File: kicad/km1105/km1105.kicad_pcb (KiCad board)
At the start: 2 copper layers, 131.7 x 80 mm, 42 parts, among them J1 CONN-DEC-DOUBLE, J2 display_switches_hdr, J3 pgm_hdr, Q1 BC547, U1 ATtiny1616-S, U2 PCF8574T, U3 PCF8574T, U4 PCF8574T, U5 PCF8574T, U6 PCF8574T, U7 PCF8574T, U8 74ACT00SC, U9 LD1117S33TR_SOT223

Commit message: Update the display board
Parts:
- added C12: 100nF, Capacitor_SMD:C_0805_2012Metric, F.Cu at (221.7, 258.8)
- added J4: la_01, Connector_PinHeader_2.54mm:PinHeader_2x20_P2.54mm_Vertical, F.Cu at (325.9, 239.5)
- added J5: la_02, Connector_PinHeader_2.54mm:PinHeader_2x04_P2.54mm_Vertical, F.Cu at (325.6, 250.4)
- added U10: SN74LVC245APW, Package_SO:TSSOP-20_4.4x6.5mm_P0.65mm, F.Cu at (227.8, 258.6)
- C10, C11: footprint Capacitor_SMD:CP_Elec_8x5.4 -> Capacitor_SMD:CP_Elec_4x4.5
- G***: moved to B.Cu
- moved J3 30.5 mm to (252.5, 246.4)
- moved D1 15.8 mm to (267.9, 246.6)
- moved D2 15.8 mm to (267.9, 240.3)
- moved R10 15.8 mm to (262.2, 246.6)
- moved R11 15.8 mm to (262.2, 240.3)
- moved G*** 8.57 mm to (306.8, 261.1), turned to 180 degrees
- moved C10 3.82 mm to (240.8, 258.8)
- moved R2 3.05 mm to (267.1, 252.0)
- moved R5 3.05 mm to (267.1, 257.0)
- moved R7 3.05 mm to (267.1, 262.1)
- moved R8 3.05 mm to (267.1, 267.2)
- moved R1 3.05 mm to (262.0, 252.0)
- moved R4 3.05 mm to (262.0, 257.0)
- moved R6 3.05 mm to (262.0, 262.1)
- moved R9 3.05 mm to (262.0, 267.2)
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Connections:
- J2 pad 10: /LCD_CS -> GND
- J2 pad 11: /s4_off -> /LCD_SCK
- J2 pad 12: /LCD_DC -> GND
- J2 pad 13: /s4_on -> /LCD_MOSI
- J2 pad 14: /LCD_RST -> GND
- J2 pad 15: /+3.3V -> /LCD_RST
- J2 pad 16: /PB4 -> GND
- J2 pad 17: /+3.3V -> /LCD_DC
- J2 pad 18: /PB5 -> GND
- J2 pad 19: GND -> /LCD_CS
- J2 pad 2: +5V -> /+3.3V
- J2 pad 4: /LCD_SDA_MOSI -> /+3.3V
- J2 pad 6: /MISO -> /s4_off
- J2 pad 8: /LCD_SCK -> /s4_on
- R7 pad 2: /s4_off -> /s4_on
- R9 pad 2: /s4_on -> /s4_off
- U1 pad 17: /LCD_SDA_MOSI -> /LCDU_MOSI
- U1 pad 19: /LCD_SCK -> /LCDU_SCK
- U1 pad 2: /LCD_CS -> /LCDU_CS
- U1 pad 8: /LCD_RST -> /LCDU_RST
- U1 pad 9: /LCD_DC -> /LCDU_DC
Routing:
- net /BSR14_H_2: track 42.0 -> 173.4 mm, vias 1 -> 4
- net /BSR7_H_2: track 31.3 -> 154.8 mm, vias 1 -> 2
- net /C_H_2: track 13.8 -> 134.0 mm
- net /BSR12_H_2: track 33.2 -> 153.2 mm, vias 1 -> 5
- net /BSR8_H_2: track 31.8 -> 148.8 mm, vias 1 -> 4
- net /BSR15_H_2: track 19.0 -> 132.1 mm, vias 1 -> 2
- net /ISR1_H_2: track 25.5 -> 131.0 mm, vias 1 -> 2
- net /ISR7_H: track 17.5 -> 120.3 mm, vias 2 -> 4
- net /V_H_2: track 16.3 -> 118.9 mm, vias 2 -> 4
- net /Z_H_2: track 29.3 -> 130.1 mm, vias 2 -> 6
- net /BSR3_H_2: track 61.2 -> 156.6 mm, vias 2 -> 6
- net /ISR1_H: track 44.4 -> 133.8 mm, vias 1 -> 2
- net /N_H_2: track 39.5 -> 127.1 mm, vias 2 -> 4
- net /ISR2_H: track 13.2 -> 98.7 mm, vias 1 -> 4
- net /ISR7_H_2: track 28.4 -> 111.4 mm, vias 2 -> 3
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
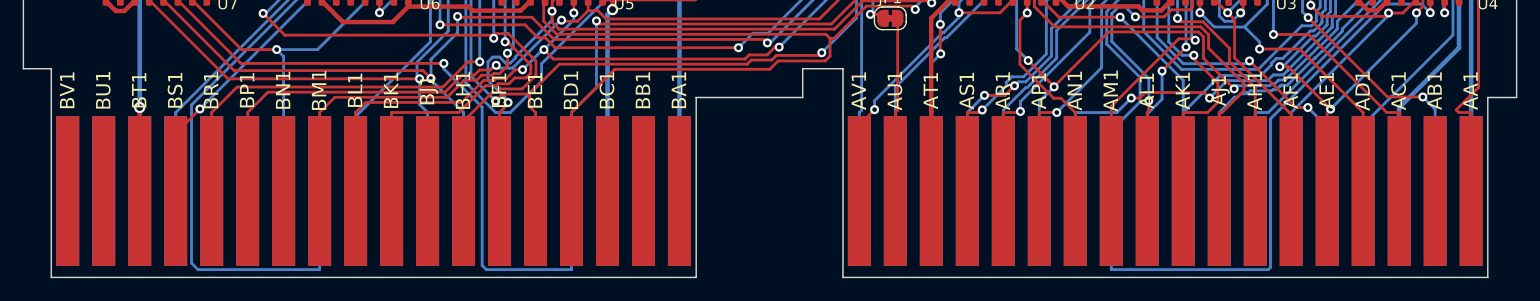
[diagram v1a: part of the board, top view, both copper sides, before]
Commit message: Fix documentation according to latest layout; fix edge connectors with chamfers
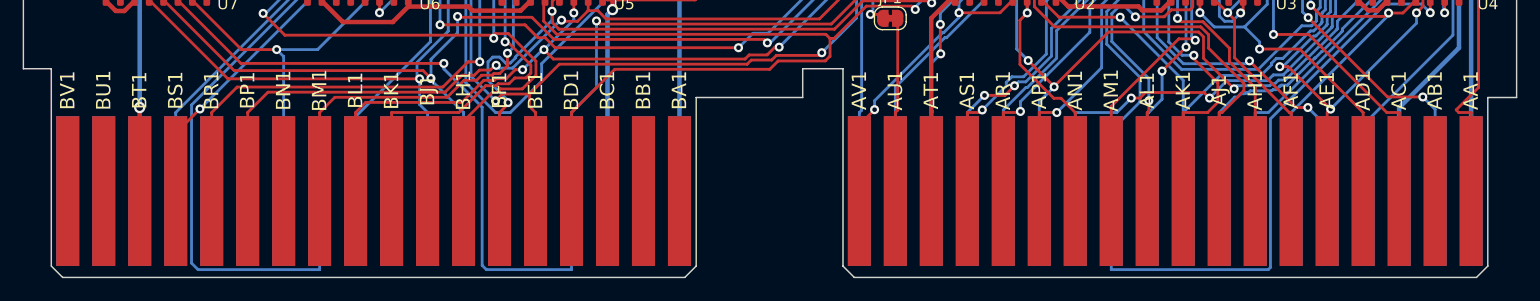
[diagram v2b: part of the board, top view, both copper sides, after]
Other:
- outline, holes or cut-outs redrawn
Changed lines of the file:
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@@
 	(paper "C")
 	(title_block
-		(title "DEC FLIP CHIP Module : DOUBLE-HEIGHT, EXTENDED-LENGTH")
+		(title "KM11 mainboard")
+		(date "2026-09-20")
 		(rev "1")
+		(company "ErrorSoft")
 	)
 	(layers
@@
 	(gr_line
 		(start 200.914 286.385)
-		(end 200.914 304.8)
+		(end 200.914 303.8)
+		(stroke
+			(width 0.127)
+			(type solid)
+		)
+		(layer "Edge.Cuts")
+	)
+	(gr_line
+		(start 200.914 303.8)
+		(end 201.914 304.8)
+		(stroke
+			(width 0.127)
+			(type solid)
+		)
+		(layer "Edge.Cuts")
+	)
+	(gr_line
+		(start 256.81 304.8)
+		(end 201.914 304.8)
 		(stroke
 			(width 0.127)
@@
 	(gr_line
 		(start 257.81 288.925)
-		(end 257.81 304.8)
+		(end 257.81 303.8)
 		(stroke
 			(width 0.127)
@@
 	)
 	(gr_line
-		(start 257.81 304.8)
-		(end 200.914 304.8)
+		(start 257.81 303.8)
+		(end 256.81 304.8)
 		(stroke
 			(width 0.127)
@@
 	(gr_line
 		(start 270.764 286.385)
-		(end 270.764 304.8)
+		(end 270.764 303.8)
+		(stroke
+			(width 0.127)
+			(type solid)
+		)
+		(layer "Edge.Cuts")
+	)
+	(gr_line
+		(start 270.764 303.8)
+		(end 271.764 304.8)
+		(stroke
+			(width 0.127)
+			(type solid)
+		)
+		(layer "Edge.Cuts")
+	)
+	(gr_line
+		(start 326.66 304.8)
+		(end 271.764 304.8)
 		(stroke
 			(width 0.127)
@@
 	(gr_line
 		(start 327.66 288.925)
-		(end 327.66 304.8)
+		(end 327.66 303.8)
 		(stroke
 			(width 0.127)
@@
 	)
 	(gr_line
-		(start 327.66 304.8)
-		(end 270.764 304.8)
+		(start 327.66 303.8)
+		(end 326.66 304.8)
 		(stroke
 			(width 0.127)

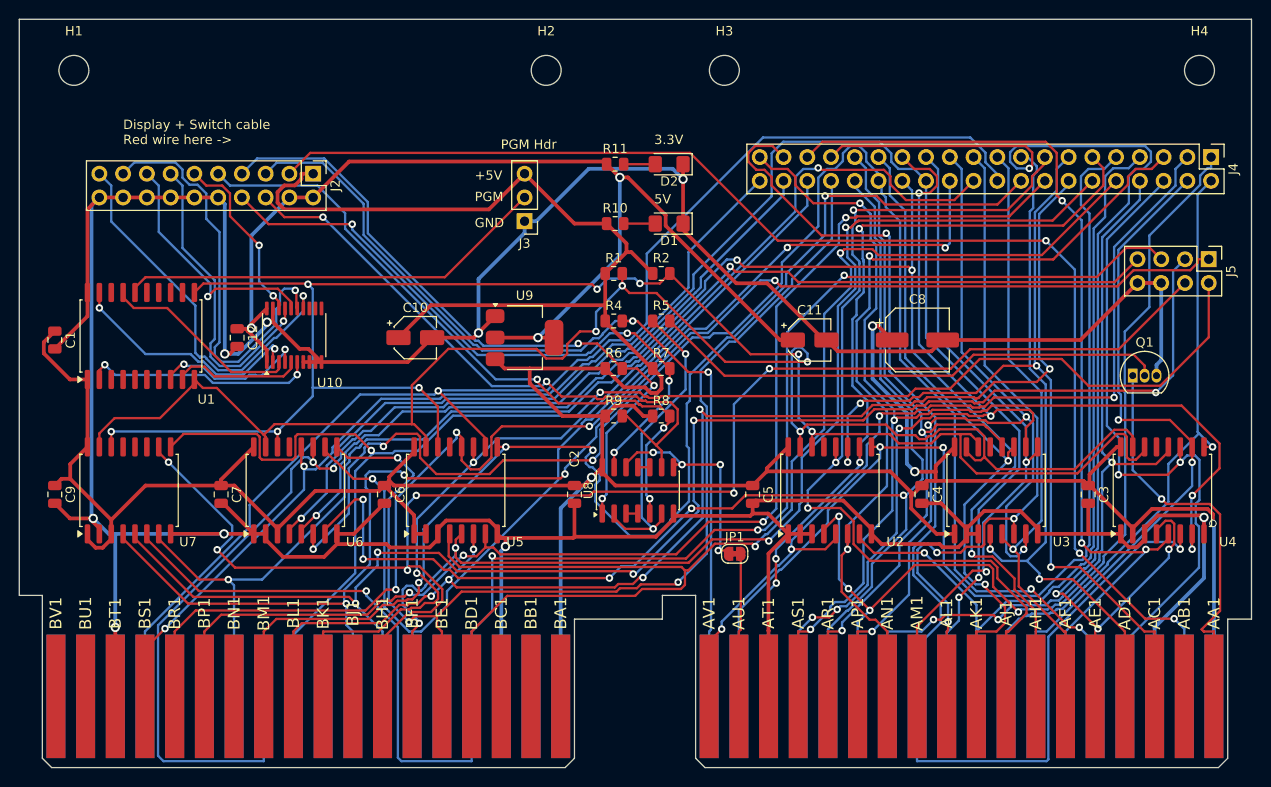
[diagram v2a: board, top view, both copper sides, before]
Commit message: Remove debug from screen
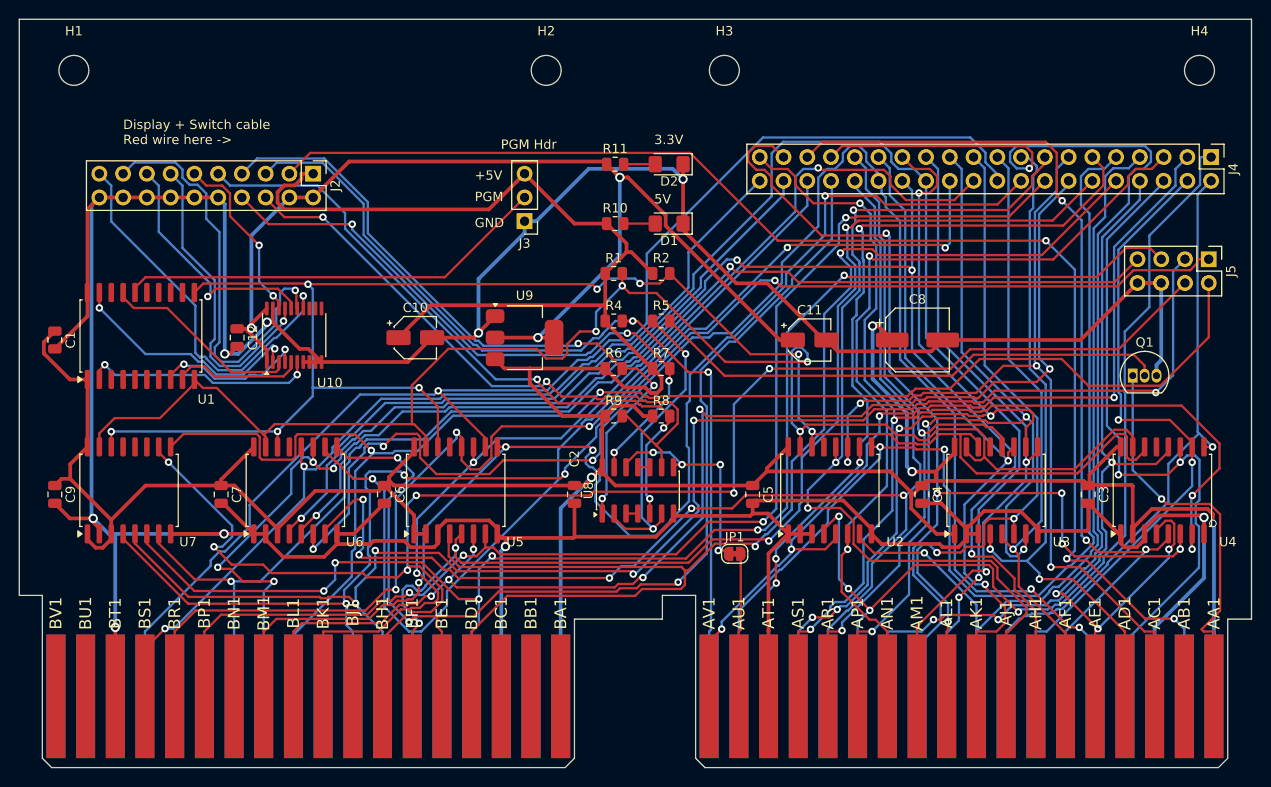
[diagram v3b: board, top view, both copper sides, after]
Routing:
- net /ISR1_H_2: track 131.0 -> 97.4 mm, vias 2 -> 4
- net /ISR1_H: track 133.8 -> 107.6 mm, vias 2 -> 5
- net /BSR14_H_2: track 173.4 -> 149.7 mm, vias 4 -> 6
- net +5V: track 397.2 -> 400.0 mm
- net GND: track 467.3 -> 469.2 mm
- net /TIMEOUT_H: track 136.5 -> 138.4 mm
- net /BSR3_H_2: track 156.6 -> 158.1 mm
- net /BSR12_H_2: track 153.2 -> 154.0 mm
- net /ISR0_H_2: track 92.5 -> 93.0 mm
